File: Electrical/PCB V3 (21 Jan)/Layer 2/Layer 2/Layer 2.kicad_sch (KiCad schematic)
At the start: 86 parts, among them J1 XT60-M, J2 Conn_02x04_Odd_Even, J3 Conn_01x04, J5 Conn_01x02, Q1 AON6354, Q2 AON6354, Q3 AON6354, Q4 AON6354, SW2 SW_SPST, SW3 SW_SPST, U1 VNH5019ATR-E, U12 VNH5019ATR-E, U2 TPS5430DDAG4, U3 TPS5430DDAG4, U4 XT30UPB-M, U5 VNH5019ATR-E, U6 XT30UPB-M, U7 XT30UPB-M, U8 XT30UPB-M, U9 VNH5019ATR-E

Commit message: did buckies
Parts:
- C1, C3: footprint Capacitor_SMD:C_0603_1608Metric_Pad1.08x0.95mm_HandSolder -> Capacitor_SMD:C_0603_1608Metric
- R10, R11: footprint Sen Robo:res0603 -> Capacitor_SMD:C_0603_1608Metric
- R28, R37: footprint Resistor_SMD:R_0603_1608Metric -> Capacitor_SMD:C_0603_1608Metric
- TP1: footprint Custom Testpointverycool:14 AWG Testpoint (Vertical) -> Custom Testpointverycool:14 AWG Testpoint (Compact)
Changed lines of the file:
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@@
 	(label "Motor Driver"
 		(at 317.5 123.19 0)
+		(fields_autoplaced yes)
 		(effects
 			(font
@@
 	(label "Motor 1 EN B"
 		(at 171.45 52.07 0)
+		(fields_autoplaced yes)
 		(effects
 			(font
@@
 	(label "Motor 3 Out B"
 		(at 152.4 199.39 180)
+		(fields_autoplaced yes)
 		(effects
 			(font
@@
 	(label "Motor 2 EN B"
 		(at 171.45 57.15 0)
+		(fields_autoplaced yes)
 		(effects
 			(font
@@
 	(label "Motor 4 EN A"
 		(at 171.45 64.77 0)
+		(fields_autoplaced yes)
 		(effects
 			(font
@@
 	(label "Motor 1 EN A"
 		(at 26.67 128.27 0)
+		(fields_autoplaced yes)
 		(effects
 			(font
@@
 	(label "PWM Motor 4"
 		(at 171.45 80.01 0)
+		(fields_autoplaced yes)
 		(effects
 			(font
@@
 	(label "PWM Motor 2"
 		(at 120.65 140.97 0)
+		(fields_autoplaced yes)
 		(effects
 			(font
@@
 	(label "Motor 2 EN B"
 		(at 123.19 133.35 0)
+		(fields_autoplaced yes)
 		(effects
 			(font
@@
 	(label "Motor Driver"
 		(at 123.19 121.92 0)
+		(fields_autoplaced yes)
 		(effects
 			(font
@@
 	(label "Motor 2 Out A"
 		(at 177.8 179.07 180)
+		(fields_autoplaced yes)
 		(effects
 			(font
@@
 	(label "Motor 2 EN A"
 		(at 123.19 128.27 0)
+		(fields_autoplaced yes)
 		(effects
 			(font
@@
 	(label "Motor 1 Out B"
 		(at 96.52 133.35 180)
+		(fields_autoplaced yes)
 		(effects
 			(font
@@
 	(label "GND"
 		(at 171.45 82.55 0)
+		(fields_autoplaced yes)
 		(effects
 			(font
@@
 	(label "L1 RX"
 		(at 171.45 62.23 0)
+		(fields_autoplaced yes)
 		(effects
 			(font
@@
 	(label "RX (IMU)"
 		(at 135.89 57.15 180)
+		(fields_autoplaced yes)
 		(effects
 			(font
@@
 	(label "Motor 2 Out A"
 		(at 193.04 128.27 180)
+		(fields_autoplaced yes)
 		(effects
 			(font
@@
 	(label "PWM Motor 2"
 		(at 171.45 74.93 0)
+		(fields_autoplaced yes)
 		(effects
 			(font
@@
 	(label "Motor 4 Out A"
 		(at 387.35 129.54 180)
+		(fields_autoplaced yes)
 		(effects
 			(font
@@
 	(label "Motor 1 Out A"
 		(at 96.52 128.27 180)
+		(fields_autoplaced yes)
 		(effects
 			(font
@@
 	(label "TX (L3 ESP 32)"
 		(at 135.89 67.31 180)
+		(fields_autoplaced yes)
 		(effects
 			(font
@@
 	(label "Motor 2 Out B"
 		(at 193.04 133.35 180)
+		(fields_autoplaced yes)
 		(effects
 			(font
@@
 	(label "Motor 1 Out B"
 		(at 152.4 182.88 180)
+		(fields_autoplaced yes)
 		(effects
 			(font
@@
 	(label "TX (IMU)"
 		(at 135.89 59.69 180)
+		(fields_autoplaced yes)
 		(effects
 			(font
@@
 	(label "Motor 4 Out B"
 		(at 179.07 198.12 180)
+		(fields_autoplaced yes)
 		(effects
 			(font
@@
 	(label "Motor Driver"
 		(at 218.44 119.38 0)
+		(fields_autoplaced yes)
 		(effects
 			(font
@@
 	(label "RX (CAM)"
 		(at 135.89 54.61 180)
+		(fields_autoplaced yes)
 		(effects
 			(font
@@
 	(label "TX (L3 ESP 32)"
 		(at 72.39 185.42 0)
+		(fields_autoplaced yes)
 		(effects
 			(font
@@
 	(label "Motor 1 EN A"
 		(at 171.45 49.53 0)
+		(fields_autoplaced yes)
 		(effects
 			(font
@@
 	(label "Motor 3 EN B"
 		(at 135.89 74.93 180)
+		(fields_autoplaced yes)
 		(effects
 			(font
@@
 	(label "PWM Motor 3"
 		(at 171.45 77.47 0)
+		(fields_autoplaced yes)
 		(effects
 			(font
@@
 	(label "Motor 2 EN A"
 		(at 171.45 54.61 0)
+		(fields_autoplaced yes)
 		(effects
 			(font
@@
 	(label "RX (L3 ESP 32)"
 		(at 135.89 69.85 180)
+		(fields_autoplaced yes)
 		(effects
 			(font
@@
 	(label "Motor 4 EN B"
 		(at 171.45 67.31 0)
+		(fields_autoplaced yes)
 		(effects
 			(font
@@
 	(label "Motor Driver"
 		(at 16.51 173.99 0)
+		(fields_autoplaced yes)
 		(effects
 			(font
@@
 	(label "PWM Motor 3"
 		(at 217.17 138.43 0)
+		(fields_autoplaced yes)
 		(effects
 			(font
@@
 	(label "Motor 3 EN B"
 		(at 218.44 130.81 0)
+		(fields_autoplaced yes)
 		(effects
 			(font
@@
 	(label "Motor 1 Out A"
 		(at 152.4 180.34 180)
+		(fields_autoplaced yes)
 		(effects
 			(font
@@
 	(label "Motor 3 Out A"
 		(at 289.56 125.73 180)
+		(fields_autoplaced yes)
 		(effects
 			(font
@@
 	(label "Motor 4 EN B"
 		(at 317.5 134.62 0)
+		(fields_autoplaced yes)
 		(effects
 			(font
@@
 	(label "Motor 4 Out B"
 		(at 387.35 134.62 180)
+		(fields_autoplaced yes)
 		(effects
 			(font
@@
 	(label "RX (IMU)"
 		(at 72.39 193.04 0)
+		(fields_autoplaced yes)
 		(effects
 			(font
@@
 	(label "Motor 3 EN A"
 		(at 135.89 72.39 180)
+		(fields_autoplaced yes)
 		(effects
 			(font
@@
 	(label "RX (L3 ESP 32)"
 		(at 72.39 182.88 0)
+		(fields_autoplaced yes)
 		(effects
 			(font
@@
 	(label "Motor 2 Out B"
 		(at 177.8 181.61 180)
+		(fields_autoplaced yes)
 		(effects
 			(font
@@
 	(label "Motor Driver"
 		(at 26.67 121.92 0)
+		(fields_autoplaced yes)
 		(effects
 			(font
@@
 	(label "TX (CAM)"
 		(at 135.89 52.07 180)
+		(fields_autoplaced yes)
 		(effects
 			(font
@@
 	(label "L1 TX"
 		(at 207.01 181.61 180)
+		(fields_autoplaced yes)
 		(effects
 			(font
@@
 	(label "Motor 3 EN A"
 		(at 218.44 125.73 0)
+		(fields_autoplaced yes)
 		(effects
 			(font
@@
 	(label "L1 RX"
 		(at 207.01 179.07 180)
+		(fields_autoplaced yes)
 		(effects
 			(font
@@
 	(label "PWM Motor 4"
 		(at 314.96 142.24 0)
+		(fields_autoplaced yes)
 		(effects
 			(font
@@
 	(label "L1 TX"
 		(at 171.45 59.69 0)
+		(fields_autoplaced yes)
 		(effects
 			(font
@@
 	(label "Motor 3 Out B"
 		(at 289.56 130.81 180)
+		(fields_autoplaced yes)
 		(effects
 			(font
@@
 	(label "TX (CAM)"
 		(at 72.39 190.5 0)
+		(fields_autoplaced yes)
 		(effects
 			(font
@@
 	(label "Motor 4 EN A"
 		(at 317.5 129.54 0)
+		(fields_autoplaced yes)
 		(effects
 			(font
@@
 	(label "TX (IMU)"
 		(at 72.39 195.58 0)
+		(fields_autoplaced yes)
 		(effects
 			(font
@@
 	(label "Motor 1 EN B"
 		(at 26.67 133.35 0)
+		(fields_autoplaced yes)
 		(effects
 			(font
@@
 	(label "Motor 4 Out A"
 		(at 179.07 195.58 180)
+		(fields_autoplaced yes)
 		(effects
 			(font
@@
 	(label "RX (CAM)"
 		(at 72.39 187.96 0)
+		(fields_autoplaced yes)
 		(effects
 			(font
@@
 	(label "PWM Motor 1"
 		(at 24.13 140.97 0)
+		(fields_autoplaced yes)
 		(effects
 			(font
@@
 	(label "PWM Motor 1"
 		(at 171.45 72.39 0)
+		(fields_autoplaced yes)
 		(effects
 			(font
@@
 	(label "Motor 3 Out A"
 		(at 152.4 196.85 180)
+		(fields_autoplaced yes)
 		(effects
 			(font
@@
 			)
 		)
-		(property "Footprint" "Custom Testpointverycool:14 AWG Testpoint (Vertical)"
+		(property "Footprint" "Custom Testpointverycool:14 AWG Testpoint (Compact)"
 			(at 260.35 180.34 0)
 			(effects
@@
 			)
 		)
-		(property "Footprint" "Sen Robo:res0603"
+		(property "Footprint" "Capacitor_SMD:C_0603_1608Metric"
 			(at 101.092 48.26 90)
 			(effects
@@
 			)
 		)
-		(property "Footprint" "Resistor_SMD:R_0603_1608Metric"
+		(property "Footprint" "Capacitor_SMD:C_0603_1608Metric"
 			(at 101.092 74.93 90)
 			(effects
@@
 			)
 		)
-		(property "Footprint" "Sen Robo:res0603"
+		(property "Footprint" "Capacitor_SMD:C_0603_1608Metric"
 			(at 101.092 36.83 90)
 			(effects
@@
 			)
 		)
-		(property "Footprint" "Capacitor_SMD:C_0603_1608Metric_Pad1.08x0.95mm_HandSolder"
+		(property "Footprint" "Capacitor_SMD:C_0603_1608Metric"
 			(at 28.9052 40.64 0)
 			(effects
@@
 			)
 		)
-		(property "Footprint" "Capacitor_SMD:C_0603_1608Metric_Pad1.08x0.95mm_HandSolder"
+		(property "Footprint" "Capacitor_SMD:C_0603_1608Metric"
 			(at 72.39 25.7048 0)
 			(effects
@@
 			)
 		)
-		(property "Footprint" "Resistor_SMD:R_0603_1608Metric"
+		(property "Footprint" "Capacitor_SMD:C_0603_1608Metric"
 			(at 101.092 86.36 90)
 			(effects

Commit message: fixed l2. IM A GENIUS I CREATED RULE AREA
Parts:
- added H11, H12: MountingHole, MountingHole:MountingHole_3.2mm_M3_DIN965_Pad, symbol Mechanical:MountingHole
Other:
- moved on the sheet: H1, H10, H2, H3, H4, H5, H6, H7, H8, H9

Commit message: did some more l2
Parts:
- J2: footprint Connector_JST:JST_EH_B10B-EH-A_1x10_P2.50mm_Vertical -> Connector_JST:JST_XH_B10B-XH-A_1x10_P2.50mm_Vertical
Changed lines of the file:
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@@
 			)
 		)
-		(property "Footprint" "Connector_JST:JST_EH_B10B-EH-A_1x10_P2.50mm_Vertical"
+		(property "Footprint" "Connector_JST:JST_XH_B10B-XH-A_1x10_P2.50mm_Vertical"
 			(at 93.98 187.96 0)
 			(effects
@@
 					(size 1.27 1.27)
 				)
-				(hide yes)
 			)
 		)

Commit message: how thisa is final version
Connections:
- net +12V: no longer TP1.1
- net at J1.P (POS), SW2.2 (B): now also TP1.1

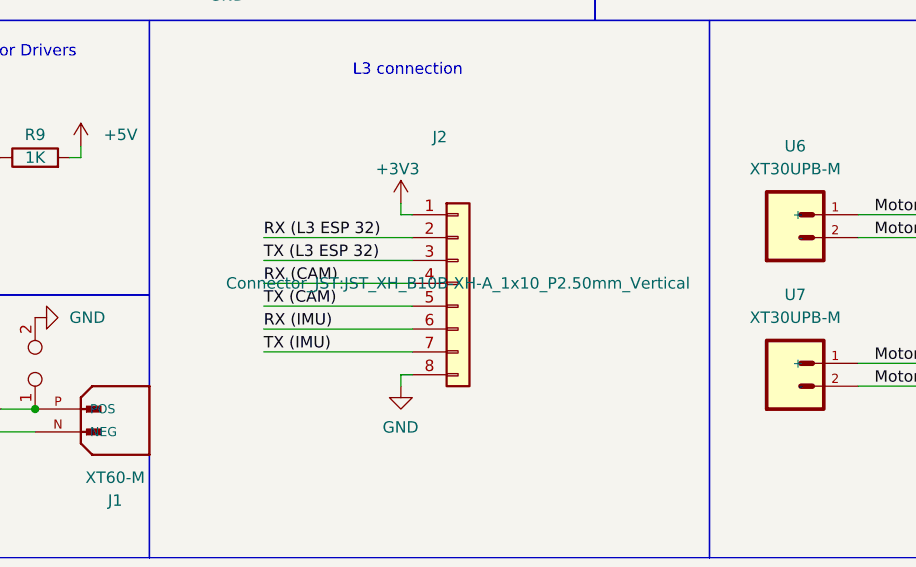
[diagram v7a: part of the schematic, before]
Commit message: fixed l2, exported new l2 and l3 steps
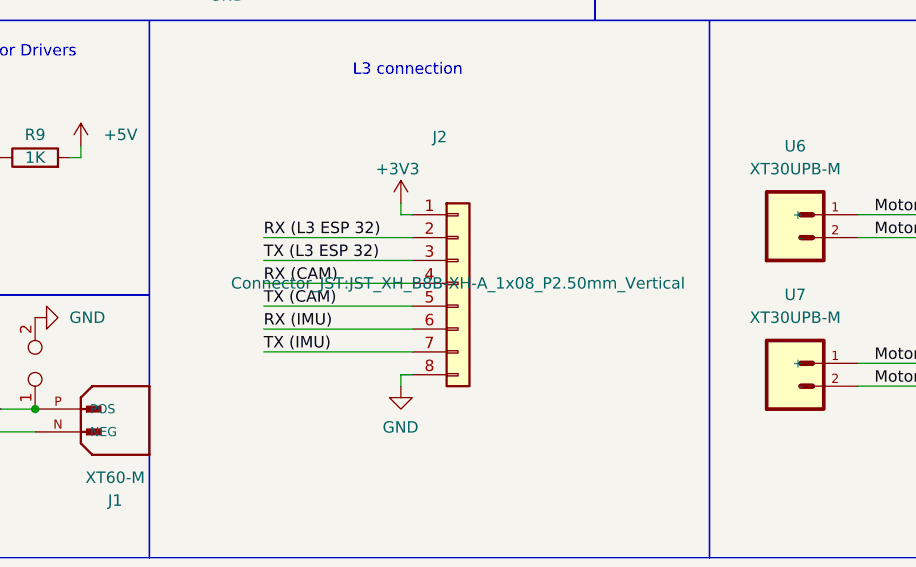
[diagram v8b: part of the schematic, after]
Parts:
- J2: footprint Connector_JST:JST_XH_B10B-XH-A_1x10_P2.50mm_Vertical -> Connector_JST:JST_XH_B8B-XH-A_1x08_P2.50mm_Vertical
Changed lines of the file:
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@@
 	(label "Motor Driver"
 		(at 317.5 123.19 0)
-		(fields_autoplaced yes)
 		(effects
 			(font
@@
 	(label "Motor 1 EN B"
 		(at 171.45 52.07 0)
-		(fields_autoplaced yes)
 		(effects
 			(font
@@
 	(label "Motor 3 Out B"
 		(at 152.4 199.39 180)
-		(fields_autoplaced yes)
 		(effects
 			(font
@@
 	(label "Motor 2 EN B"
 		(at 171.45 57.15 0)
-		(fields_autoplaced yes)
 		(effects
 			(font
@@
 	(label "Motor 4 EN A"
 		(at 171.45 64.77 0)
-		(fields_autoplaced yes)
 		(effects
 			(font
@@
 	(label "Motor 1 EN A"
 		(at 26.67 128.27 0)
-		(fields_autoplaced yes)
 		(effects
 			(font
@@
 	(label "PWM Motor 4"
 		(at 171.45 80.01 0)
-		(fields_autoplaced yes)
 		(effects
 			(font
@@
 	(label "PWM Motor 2"
 		(at 120.65 140.97 0)
-		(fields_autoplaced yes)
 		(effects
 			(font
@@
 	(label "Motor 2 EN B"
 		(at 123.19 133.35 0)
-		(fields_autoplaced yes)
 		(effects
 			(font
@@
 	(label "Motor Driver"
 		(at 123.19 121.92 0)
-		(fields_autoplaced yes)
 		(effects
 			(font
@@
 	(label "Motor 2 Out A"
 		(at 177.8 179.07 180)
-		(fields_autoplaced yes)
 		(effects
 			(font
@@
 	(label "Motor 2 EN A"
 		(at 123.19 128.27 0)
-		(fields_autoplaced yes)
 		(effects
 			(font
@@
 	(label "Motor 1 Out B"
 		(at 96.52 133.35 180)
-		(fields_autoplaced yes)
 		(effects
 			(font
@@
 	(label "GND"
 		(at 171.45 82.55 0)
-		(fields_autoplaced yes)
 		(effects
 			(font
@@
 	(label "L1 RX"
 		(at 171.45 62.23 0)
-		(fields_autoplaced yes)
 		(effects
 			(font
@@
 	(label "RX (IMU)"
 		(at 135.89 57.15 180)
-		(fields_autoplaced yes)
 		(effects
 			(font
@@
 	(label "Motor 2 Out A"
 		(at 193.04 128.27 180)
-		(fields_autoplaced yes)
 		(effects
 			(font
@@
 	(label "PWM Motor 2"
 		(at 171.45 74.93 0)
-		(fields_autoplaced yes)
 		(effects
 			(font
@@
 	(label "Motor 4 Out A"
 		(at 387.35 129.54 180)
-		(fields_autoplaced yes)
 		(effects
 			(font
@@
 	(label "Motor 1 Out A"
 		(at 96.52 128.27 180)
-		(fields_autoplaced yes)
 		(effects
 			(font
@@
 	(label "TX (L3 ESP 32)"
 		(at 135.89 67.31 180)
-		(fields_autoplaced yes)
 		(effects
 			(font
@@
 	(label "Motor 2 Out B"
 		(at 193.04 133.35 180)
-		(fields_autoplaced yes)
 		(effects
 			(font
@@
 	(label "Motor 1 Out B"
 		(at 152.4 182.88 180)
-		(fields_autoplaced yes)
 		(effects
 			(font
@@
 	(label "TX (IMU)"
 		(at 135.89 59.69 180)
-		(fields_autoplaced yes)
 		(effects
 			(font
@@
 	(label "Motor 4 Out B"
 		(at 179.07 198.12 180)
-		(fields_autoplaced yes)
 		(effects
 			(font
@@
 	(label "Motor Driver"
 		(at 218.44 119.38 0)
-		(fields_autoplaced yes)
 		(effects
 			(font
@@
 	(label "RX (CAM)"
 		(at 135.89 54.61 180)
-		(fields_autoplaced yes)
 		(effects
 			(font
@@
 	(label "TX (L3 ESP 32)"
 		(at 72.39 185.42 0)
-		(fields_autoplaced yes)
 		(effects
 			(font
@@
 	(label "Motor 1 EN A"
 		(at 171.45 49.53 0)
-		(fields_autoplaced yes)
 		(effects
 			(font
@@
 	(label "Motor 3 EN B"
 		(at 135.89 74.93 180)
-		(fields_autoplaced yes)
 		(effects
 			(font
@@
 	(label "PWM Motor 3"
 		(at 171.45 77.47 0)
-		(fields_autoplaced yes)
 		(effects
 			(font
@@
 	(label "Motor 2 EN A"
 		(at 171.45 54.61 0)
-		(fields_autoplaced yes)
 		(effects
 			(font
@@
 	(label "RX (L3 ESP 32)"
 		(at 135.89 69.85 180)
-		(fields_autoplaced yes)
 		(effects
 			(font
@@
 	(label "Motor 4 EN B"
 		(at 171.45 67.31 0)
-		(fields_autoplaced yes)
 		(effects
 			(font
@@
 	(label "Motor Driver"
 		(at 16.51 173.99 0)
-		(fields_autoplaced yes)
 		(effects
 			(font
@@
 	(label "PWM Motor 3"
 		(at 217.17 138.43 0)
-		(fields_autoplaced yes)
 		(effects
 			(font
@@
 	(label "Motor 3 EN B"
 		(at 218.44 130.81 0)
-		(fields_autoplaced yes)
 		(effects
 			(font
@@
 	(label "Motor 1 Out A"
 		(at 152.4 180.34 180)
-		(fields_autoplaced yes)
 		(effects
 			(font
@@
 	(label "Motor 3 Out A"
 		(at 289.56 125.73 180)
-		(fields_autoplaced yes)
 		(effects
 			(font
@@
 	(label "Motor 4 EN B"
 		(at 317.5 134.62 0)
-		(fields_autoplaced yes)
 		(effects
 			(font
@@
 	(label "Motor 4 Out B"
 		(at 387.35 134.62 180)
-		(fields_autoplaced yes)
 		(effects
 			(font
@@
 	(label "RX (IMU)"
 		(at 72.39 193.04 0)
-		(fields_autoplaced yes)
 		(effects
 			(font
@@
 	(label "Motor 3 EN A"
 		(at 135.89 72.39 180)
-		(fields_autoplaced yes)
 		(effects
 			(font
@@
 	(label "RX (L3 ESP 32)"
 		(at 72.39 182.88 0)
-		(fields_autoplaced yes)
 		(effects
 			(font
@@
 	(label "Motor 2 Out B"
 		(at 177.8 181.61 180)
-		(fields_autoplaced yes)
 		(effects
 			(font
@@
 	(label "Motor Driver"
 		(at 26.67 121.92 0)
-		(fields_autoplaced yes)
 		(effects
 			(font
@@
 	(label "TX (CAM)"
 		(at 135.89 52.07 180)
-		(fields_autoplaced yes)
 		(effects
 			(font
@@
 	(label "L1 TX"
 		(at 207.01 181.61 180)
-		(fields_autoplaced yes)
 		(effects
 			(font
@@
 	(label "Motor 3 EN A"
 		(at 218.44 125.73 0)
-		(fields_autoplaced yes)
 		(effects
 			(font
@@
 	(label "L1 RX"
 		(at 207.01 179.07 180)
-		(fields_autoplaced yes)
 		(effects
 			(font
@@
 	(label "PWM Motor 4"
 		(at 314.96 142.24 0)
-		(fields_autoplaced yes)
 		(effects
 			(font
@@
 	(label "L1 TX"
 		(at 171.45 59.69 0)
-		(fields_autoplaced yes)
 		(effects
 			(font
@@
 	(label "Motor 3 Out B"
 		(at 289.56 130.81 180)
-		(fields_autoplaced yes)
 		(effects
 			(font
@@
 	(label "TX (CAM)"
 		(at 72.39 190.5 0)
-		(fields_autoplaced yes)
 		(effects
 			(font
@@
 	(label "Motor 4 EN A"
 		(at 317.5 129.54 0)
-		(fields_autoplaced yes)
 		(effects
 			(font
@@
 	(label "TX (IMU)"
 		(at 72.39 195.58 0)
-		(fields_autoplaced yes)
 		(effects
 			(font
@@
 	(label "Motor 1 EN B"
 		(at 26.67 133.35 0)
-		(fields_autoplaced yes)
 		(effects
 			(font
@@
 	(label "Motor 4 Out A"
 		(at 179.07 195.58 180)
-		(fields_autoplaced yes)
 		(effects
 			(font
@@
 	(label "RX (CAM)"
 		(at 72.39 187.96 0)
-		(fields_autoplaced yes)
 		(effects
 			(font
@@
 	(label "PWM Motor 1"
 		(at 24.13 140.97 0)
-		(fields_autoplaced yes)
 		(effects
 			(font
@@
 	(label "PWM Motor 1"
 		(at 171.45 72.39 0)
-		(fields_autoplaced yes)
 		(effects
 			(font
@@
 	(label "Motor 3 Out A"
 		(at 152.4 196.85 180)
-		(fields_autoplaced yes)
 		(effects
 			(font
@@
 			)
 		)
-		(property "Footprint" "Connector_JST:JST_XH_B10B-XH-A_1x10_P2.50mm_Vertical"
+		(property "Footprint" "Connector_JST:JST_XH_B8B-XH-A_1x08_P2.50mm_Vertical"
 			(at 93.98 187.96 0)
 			(effects
